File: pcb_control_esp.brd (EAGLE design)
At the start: 100 x 50 mm, 45 parts, among them IC1 AT24CP, IC2 REG1117, IC4 DS3231SN, IC5 74LS595N, K1 HKE, Q1 BC337, Q2 BC337, X1 VIN

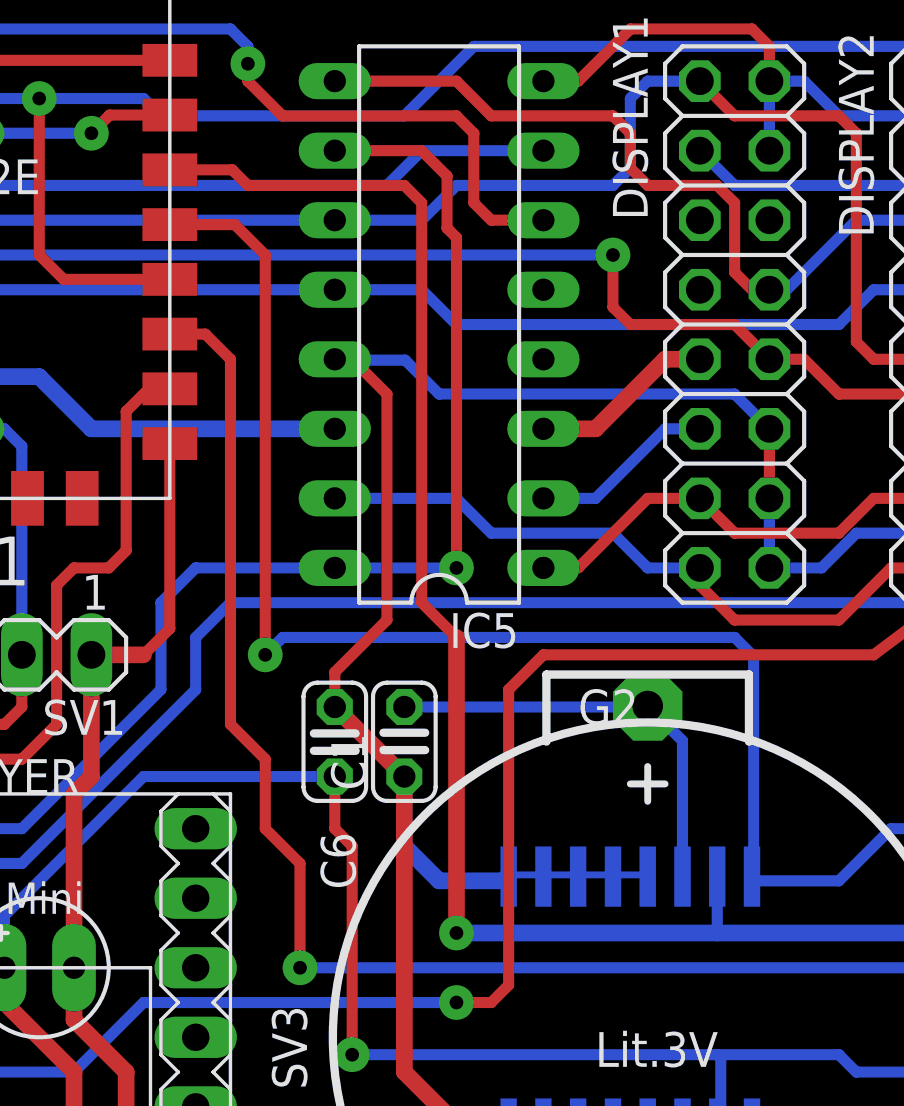
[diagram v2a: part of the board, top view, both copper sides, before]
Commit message: swap i2c
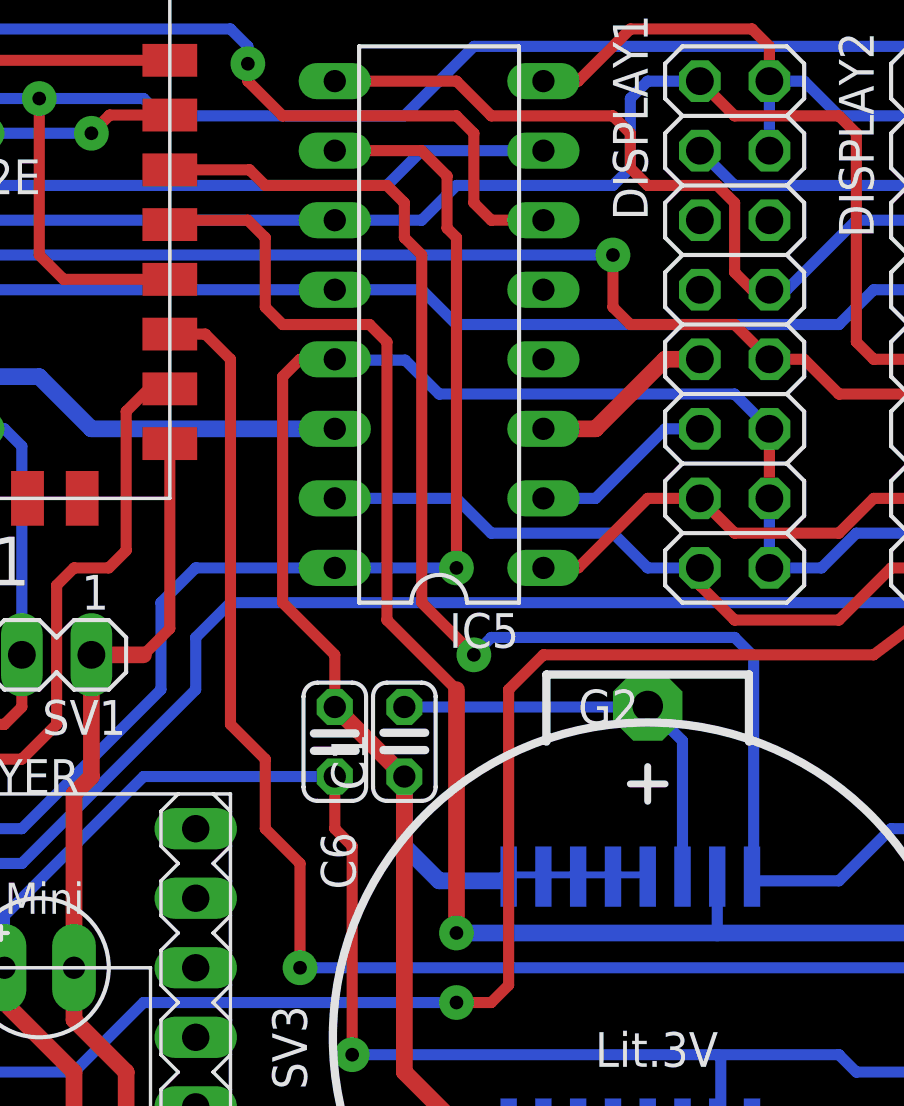
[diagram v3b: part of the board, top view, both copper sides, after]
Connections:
- net SCL: now also SJR1.14; no longer SJR1.13
- net SDA: now also SJR1.13; no longer SJR1.14
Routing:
- net SDA: track 75.7 -> 72.8 mm
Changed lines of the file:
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@@
 <grid distance="0.025" unitdist="inch" unit="mm" style="lines" multiple="1" display="yes" altdistance="0.025" altunitdist="inch" altunit="inch"/>
 <layers>
-<layer number="1" name="Top" color="4" fill="1" visible="no" active="yes"/>
+<layer number="1" name="Top" color="4" fill="1" visible="yes" active="yes"/>
 <layer number="2" name="Route2" color="1" fill="3" visible="no" active="no"/>
 <layer number="3" name="Route3" color="4" fill="3" visible="no" active="no"/>
@@
 <wire x1="74.8" y1="18" x2="74.93" y2="17.935" width="0.254" layer="16"/>
 <wire x1="73.6" y1="18" x2="73.66" y2="17.935" width="0.254" layer="16"/>
-<wire x1="63.6" y1="36.8" x2="63.5" y2="36.83" width="0.254" layer="1"/>
 <wire x1="69.6" y1="18" x2="69.85" y2="17.935" width="0.254" layer="16"/>
 <wire x1="96.4" y1="29.2" x2="95.2" y2="29.2" width="0.254" layer="16"/>
@@
 <wire x1="57.475" y1="33.75" x2="57.475" y2="26.995" width="0.4064" layer="1"/>
 <wire x1="57.475" y1="26.995" x2="56.515" y2="26.035" width="0.4064" layer="1"/>
-<wire x1="63.6" y1="36.8" x2="64.165" y2="36.8" width="0.4064" layer="1"/>
-<wire x1="64.165" y1="36.8" x2="65.405" y2="35.56" width="0.4064" layer="1"/>
-<wire x1="65.405" y1="35.56" x2="65.405" y2="27.305" width="0.4064" layer="1"/>
-<wire x1="65.405" y1="27.305" x2="63.5" y2="25.4" width="0.4064" layer="1"/>
-<wire x1="63.5" y1="25.4" x2="63.5" y2="24.13" width="0.4064" layer="1"/>
+<wire x1="63.5" y1="26.035" x2="63.5" y2="24.13" width="0.4064" layer="1"/>
 <wire x1="20.32" y1="18.415" x2="13.335" y2="18.415" width="0.8128" layer="16"/>
 <wire x1="13.335" y1="18.415" x2="12.065" y2="19.685" width="0.8128" layer="16"/>
@@
 <wire x1="67.31" y1="35.56" x2="78.105" y2="35.56" width="0.4064" layer="16"/>
 <wire x1="78.105" y1="35.56" x2="79.375" y2="34.29" width="0.4064" layer="16"/>
+<wire x1="63.5" y1="26.035" x2="61.595" y2="27.94" width="0.4064" layer="1"/>
+<wire x1="61.595" y1="27.94" x2="61.595" y2="36.195" width="0.4064" layer="1"/>
+<wire x1="61.595" y1="36.195" x2="62.23" y2="36.83" width="0.4064" layer="1"/>
+<wire x1="62.23" y1="36.83" x2="63.5" y2="36.83" width="0.4064" layer="1"/>
 </signal>
 <signal name="SCL">
@@
 <contactref element="R5" pad="1"/>
 <contactref element="IC1" pad="6"/>
-<contactref element="SJR1" pad="13"/>
 <wire x1="78.8" y1="18" x2="78.74" y2="17.935" width="0.254" layer="16"/>
 <wire x1="93.345" y1="22.225" x2="93.345" y2="16.51" width="0.6096" layer="1"/>
@@
 <wire x1="78.8" y1="18" x2="78.8" y2="25.975" width="0.4064" layer="16"/>
 <wire x1="78.8" y1="25.975" x2="78.105" y2="26.67" width="0.4064" layer="16"/>
-<wire x1="78.105" y1="26.67" x2="61.595" y2="26.67" width="0.4064" layer="16"/>
-<wire x1="61.595" y1="26.67" x2="60.96" y2="26.035" width="0.4064" layer="16"/>
-<via x="60.96" y="26.035" extent="1-16" drill="0.5" diameter="1.27"/>
-<wire x1="60.96" y1="26.035" x2="60.96" y2="40.64" width="0.4064" layer="1"/>
-<wire x1="57.475" y1="41.75" x2="59.85" y2="41.75" width="0.4064" layer="1"/>
-<wire x1="59.85" y1="41.75" x2="60.96" y2="40.64" width="0.4064" layer="1"/>
+<wire x1="78.105" y1="26.67" x2="69.215" y2="26.67" width="0.4064" layer="16"/>
+<wire x1="69.215" y1="26.67" x2="68.58" y2="26.035" width="0.4064" layer="16"/>
+<via x="68.58" y="26.035" extent="1-16" drill="0.5" diameter="1.27"/>
 <wire x1="89.535" y1="15.875" x2="91.44" y2="15.875" width="0.4064" layer="16"/>
 <wire x1="91.44" y1="15.875" x2="92.075" y2="16.51" width="0.4064" layer="16"/>
@@
 <wire x1="81.915" y1="17.78" x2="78.895" y2="17.78" width="0.4064" layer="16"/>
 <wire x1="78.895" y1="17.78" x2="78.74" y2="17.935" width="0.4064" layer="16"/>
+<contactref element="SJR1" pad="14"/>
+<wire x1="57.475" y1="43.75" x2="60.39" y2="43.75" width="0.4064" layer="1"/>
+<wire x1="60.39" y1="43.75" x2="60.96" y2="43.18" width="0.4064" layer="1"/>
+<wire x1="60.96" y1="43.18" x2="65.405" y2="43.18" width="0.4064" layer="1"/>
+<wire x1="65.405" y1="43.18" x2="66.04" y2="42.545" width="0.4064" layer="1"/>
+<wire x1="66.04" y1="42.545" x2="66.04" y2="41.275" width="0.4064" layer="1"/>
+<wire x1="66.04" y1="41.275" x2="66.675" y2="40.64" width="0.4064" layer="1"/>
+<wire x1="66.675" y1="40.64" x2="66.675" y2="27.94" width="0.4064" layer="1"/>
+<wire x1="66.675" y1="27.94" x2="68.58" y2="26.035" width="0.4064" layer="1"/>
 </signal>
 <signal name="SDA">
@@
 <contactref element="R6" pad="1"/>
 <contactref element="IC1" pad="5"/>
-<contactref element="SJR1" pad="14"/>
-<wire x1="57.475" y1="43.75" x2="59.755" y2="43.75" width="0.4064" layer="1"/>
-<wire x1="59.755" y1="43.75" x2="60.325" y2="43.18" width="0.4064" layer="1"/>
-<wire x1="60.325" y1="43.18" x2="66.04" y2="43.18" width="0.4064" layer="1"/>
-<wire x1="66.04" y1="43.18" x2="66.675" y2="42.545" width="0.4064" layer="1"/>
-<wire x1="66.675" y1="42.545" x2="66.675" y2="27.94" width="0.4064" layer="1"/>
-<wire x1="66.675" y1="27.94" x2="67.945" y2="26.67" width="0.4064" layer="1"/>
 <wire x1="97.155" y1="26.035" x2="93.345" y2="26.035" width="0.6096" layer="1"/>
 <wire x1="93.345" y1="26.035" x2="92.075" y2="24.765" width="0.6096" layer="1"/>
@@
 <via x="67.945" y="15.875" extent="1-16" drill="0.5" diameter="1.27"/>
 <wire x1="77.47" y1="15.875" x2="67.945" y2="15.875" width="0.6096" layer="16"/>
-<wire x1="67.945" y1="15.875" x2="67.945" y2="26.67" width="0.6096" layer="1"/>
+<wire x1="67.945" y1="15.875" x2="67.945" y2="24.765" width="0.6096" layer="1"/>
 <wire x1="77.47" y1="17.935" x2="77.47" y2="15.875" width="0.4064" layer="16"/>
+<contactref element="SJR1" pad="13"/>
+<wire x1="60.325" y1="41.91" x2="57.635" y2="41.91" width="0.4064" layer="1"/>
+<wire x1="57.635" y1="41.91" x2="57.475" y2="41.75" width="0.4064" layer="1"/>
+<wire x1="60.325" y1="41.91" x2="60.96" y2="41.275" width="0.4064" layer="1"/>
+<wire x1="60.96" y1="41.275" x2="60.96" y2="38.735" width="0.4064" layer="1"/>
+<wire x1="60.96" y1="38.735" x2="61.595" y2="38.1" width="0.4064" layer="1"/>
+<wire x1="61.595" y1="38.1" x2="64.77" y2="38.1" width="0.4064" layer="1"/>
+<wire x1="64.77" y1="38.1" x2="65.405" y2="37.465" width="0.4064" layer="1"/>
+<wire x1="65.405" y1="37.465" x2="65.405" y2="27.305" width="0.4064" layer="1"/>
+<wire x1="65.405" y1="27.305" x2="67.945" y2="24.765" width="0.4064" layer="1"/>
 </signal>
 <signal name="INT/SQW">
